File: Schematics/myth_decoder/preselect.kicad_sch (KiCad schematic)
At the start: 8 parts, among them U10 74HC238, U11 74HC238, U12 74LS08, U13 74AHC04, U14 4078, U15 4075, U3 74LS32, U9 74HC238

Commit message: Change d to g
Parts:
- added C1015: C 100nF, Capacitor_THT:C_Disc_D5.0mm_W2.5mm_P2.50mm, symbol Device:C_Small
- added C1016: CP 10μF, Capacitor_THT:CP_Radial_D6.3mm_P2.50mm, symbol Device:C_Polarized_Small
- renumbered U3 to U1003, U9 to U1009, U10 to U1010, U11 to U1011, U12 to U1012, U13 to U1013, U14 to U1014, U15 to U1015
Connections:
- net Vdd: now also C1015.1, C1016.1
- net Vss: now also C1015.2, C1016.2

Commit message: Update pencoder image
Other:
- note added: "NM => END (LOX) NL => NOP (reserved) LM => NOP (reserved) LL => NOP (reserved) MM => NOP (reserved) ML => NOP (reserved) GG => NOP (reserved) RR => NOP (reserved) II => NOP (reserved)"
- note added: "Remap ("scrounge") GG, RR, II etc, and impracticable opcodes such as NM"
- note removed: "NM => END (LOX) NL => NOP (reserved) LM => NOP (reserved) LL => NOP (reserved) MM => NOP (reserved) ML => NOP (reserved) DD => NOP (reserved) RR => NOP (reserved) II => NOP (reserved)"
- note removed: "Remap ("scrounge") DD, RR, II etc, and impracticable opcodes such as NM"
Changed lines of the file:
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@@
 		)
 	)
-	(text "Remap (\"scrounge\") DD, RR, II etc,\nand impracticable opcodes such as NM"
+	(text "Remap (\"scrounge\") GG, RR, II etc,\nand impracticable opcodes such as NM"
 		(exclude_from_sim no)
 		(at 138.43 65.532 0)
@@
 		)
 	)
-	(text "NM => END (LOX)\nNL => NOP (reserved)\nLM => NOP (reserved)\nLL => NOP (reserved)\nMM => NOP (reserved)\nML => NOP (reserved)\nDD => NOP (reserved)\nRR => NOP (reserved)\nII => NOP (reserved)"
+	(text "NM => END (LOX)\nNL => NOP (reserved)\nLM => NOP (reserved)\nLL => NOP (reserved)\nMM => NOP (reserved)\nML => NOP (reserved)\nGG => NOP (reserved)\nRR => NOP (reserved)\nII => NOP (reserved)"
 		(exclude_from_sim no)
 		(at 227.584 64.008 0)

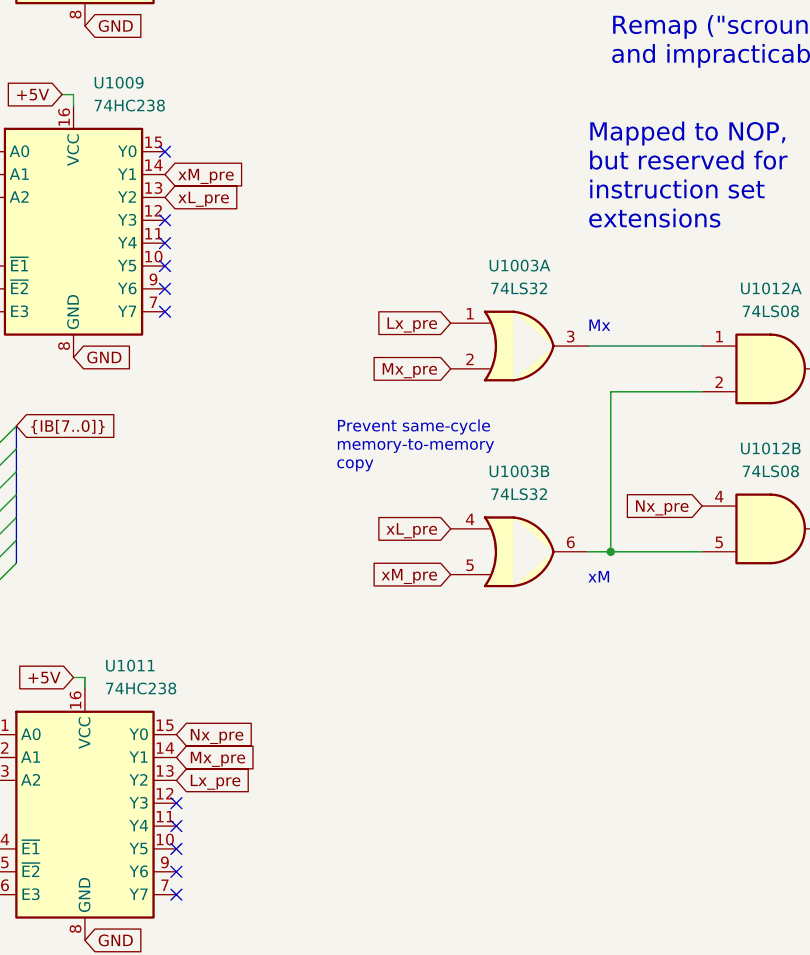
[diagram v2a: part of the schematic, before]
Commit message: Change semantics of xB
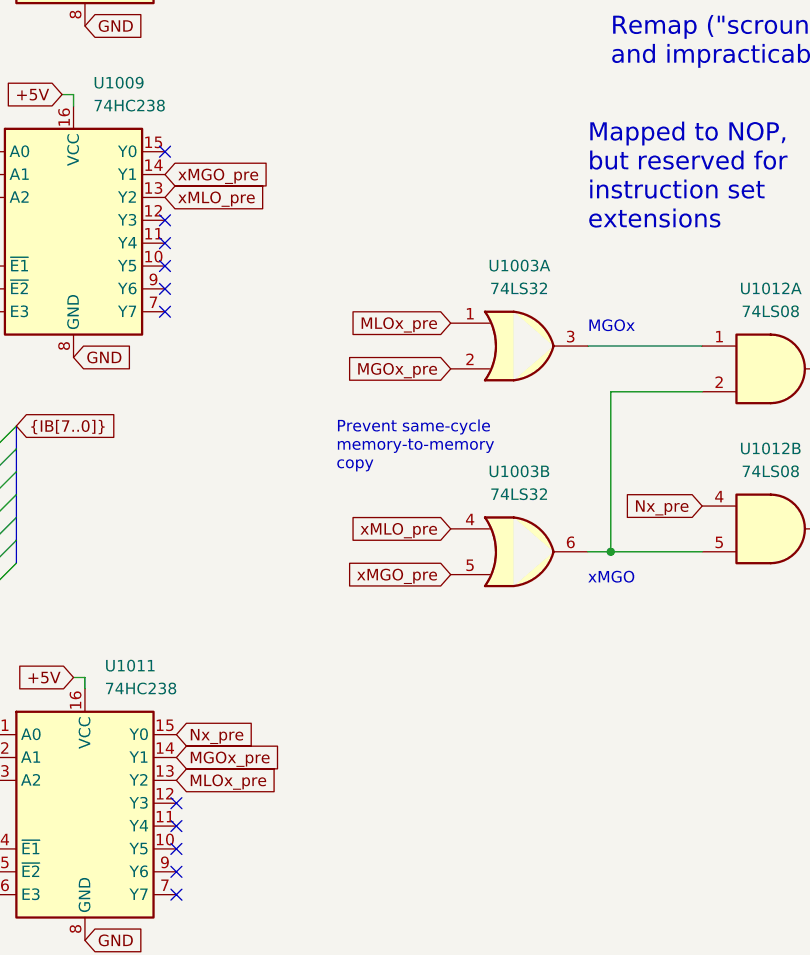
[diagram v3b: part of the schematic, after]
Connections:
- net Lx_pre renamed MLOx_pre
- net Mx_pre renamed MGOx_pre
- net xL_pre renamed xMLO_pre
- net xM_pre renamed xMGO_pre
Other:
- note added: "MGOx"
- note added: "xMGO"
- note removed: "Mx"
- note removed: "xM"
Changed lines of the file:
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@@
 		)
 	)
-	(text "Mx"
+	(text "MGOx"
 		(exclude_from_sim no)
 		(at 135.89 95.25 0)
@@
 		)
 	)
-	(text "xM"
+	(text "xMGO"
 		(exclude_from_sim no)
 		(at 135.89 123.19 0)
@@
 		)
 	)
-	(global_label "Mx_pre"
+	(global_label "MGOx_pre"
 		(shape input)
 		(at 90.17 142.24 0)
@@
 		)
 	)
-	(global_label "Mx_pre"
+	(global_label "MGOx_pre"
 		(shape input)
 		(at 120.65 99.06 180)
@@
 		)
 	)
-	(global_label "Lx_pre"
+	(global_label "MLOx_pre"
 		(shape input)
 		(at 90.17 144.78 0)
@@
 		)
 	)
-	(global_label "xL_pre"
+	(global_label "xMLO_pre"
 		(shape input)
 		(at 88.9 80.01 0)
@@
 		)
 	)
-	(global_label "xM_pre"
+	(global_label "xMGO_pre"
 		(shape input)
 		(at 88.9 77.47 0)
@@
 		)
 	)
-	(global_label "xL_pre"
+	(global_label "xMLO_pre"
 		(shape input)
 		(at 120.65 116.84 180)
@@
 		)
 	)
-	(global_label "xM_pre"
+	(global_label "xMGO_pre"
 		(shape input)
 		(at 120.65 121.92 180)
@@
 		)
 	)
-	(global_label "Lx_pre"
+	(global_label "MLOx_pre"
 		(shape input)
 		(at 120.65 93.98 180)

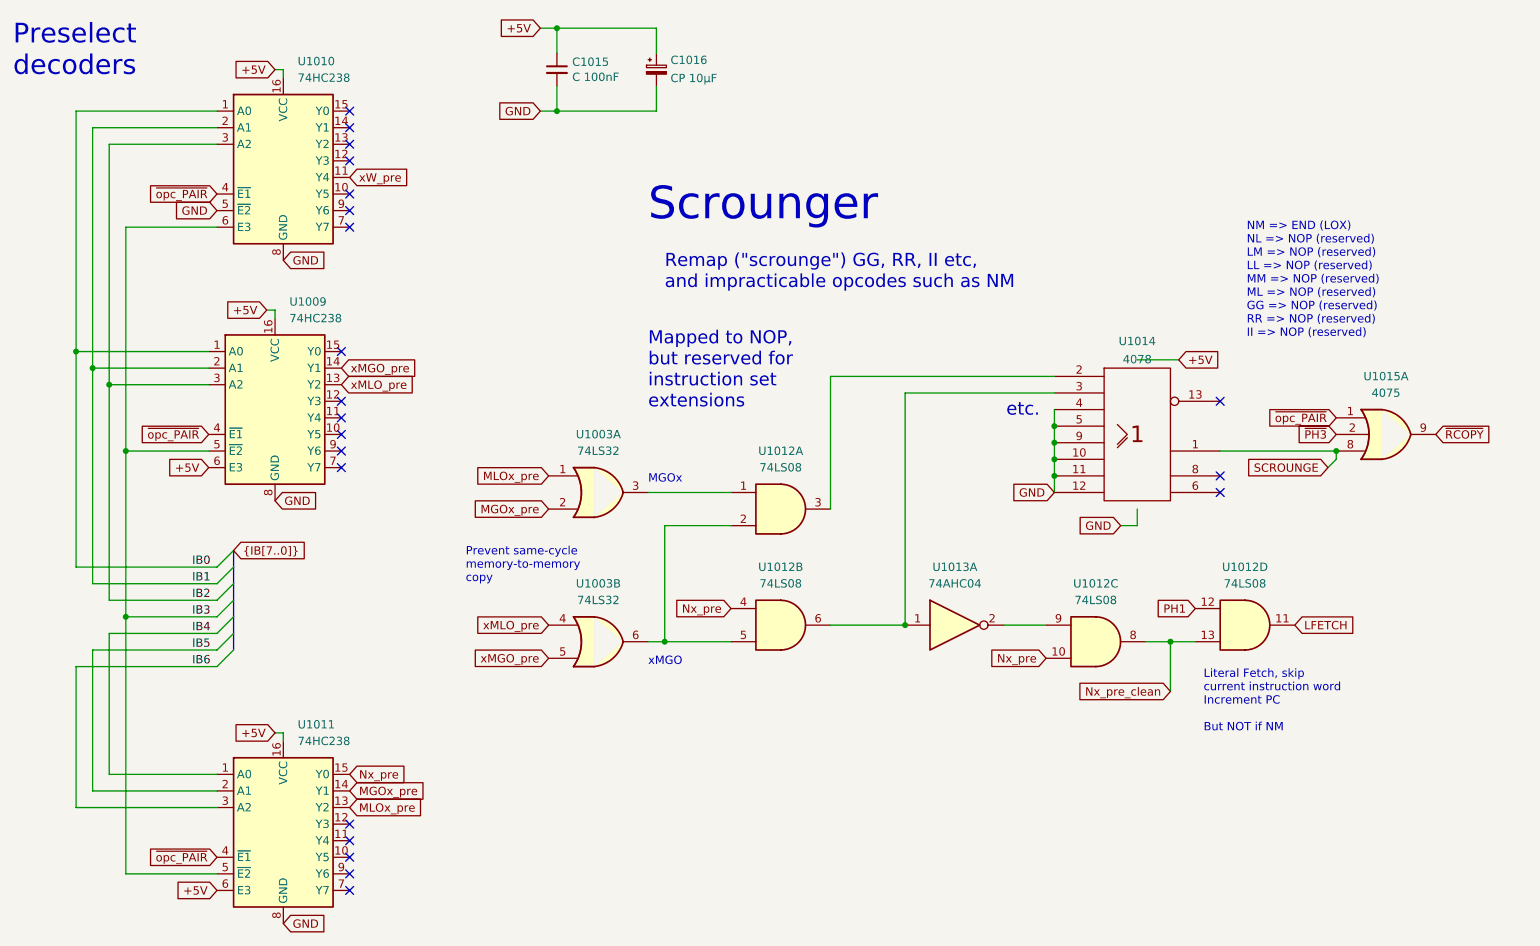
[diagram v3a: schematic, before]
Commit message: Change signal names
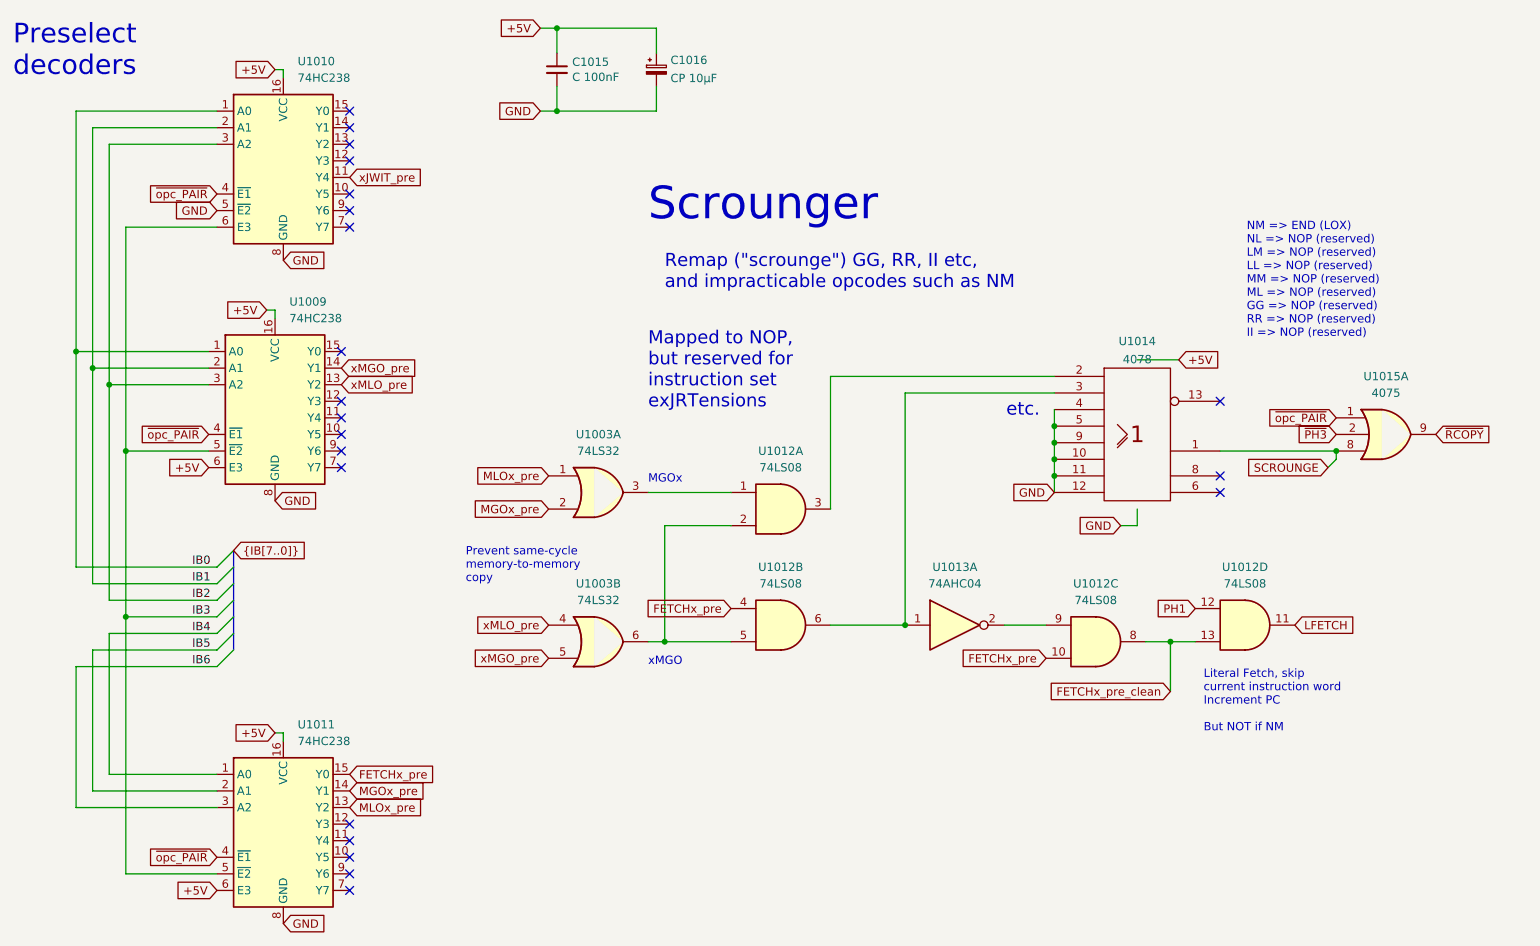
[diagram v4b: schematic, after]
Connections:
- net Nx_pre renamed FETCHx_pre
- net Nx_pre_clean renamed FETCHx_pre_clean
- net xW_pre renamed xJWIT_pre
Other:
- note added: "Mapped to NOP, but reserved for instruction set exJRTensions"
- note removed: "Mapped to NOP, but reserved for instruction set extensions"
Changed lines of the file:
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@@
 		)
 	)
-	(text "Mapped to NOP,\nbut reserved for\ninstruction set\nextensions"
+	(text "Mapped to NOP,\nbut reserved for\ninstruction set\nexJRTensions"
 		(exclude_from_sim no)
 		(at 135.89 83.82 0)
@@
 		)
 	)
-	(global_label "Nx_pre"
+	(global_label "FETCHx_pre"
 		(shape input)
 		(at 196.85 121.92 180)
@@
 		)
 	)
-	(global_label "xW_pre"
+	(global_label "xJWIT_pre"
 		(shape input)
 		(at 90.17 48.26 0)
@@
 		)
 	)
-	(global_label "Nx_pre"
+	(global_label "FETCHx_pre"
 		(shape input)
 		(at 148.59 114.3 180)
@@
 		)
 	)
-	(global_label "Nx_pre"
+	(global_label "FETCHx_pre"
 		(shape input)
 		(at 90.17 139.7 0)
@@
 		)
 	)
-	(global_label "Nx_pre_clean"
+	(global_label "FETCHx_pre_clean"
 		(shape input)
 		(at 215.9 127 180)

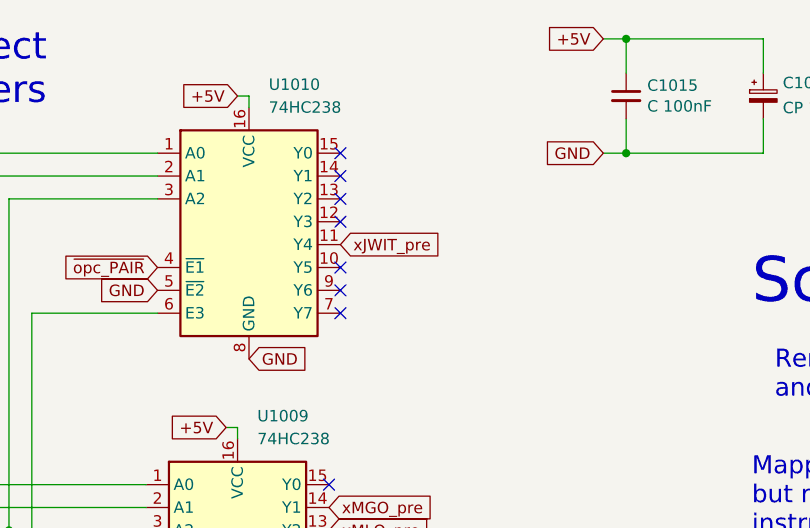
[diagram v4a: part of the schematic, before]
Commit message: Let defines/labels diverge from assembler mnemonics
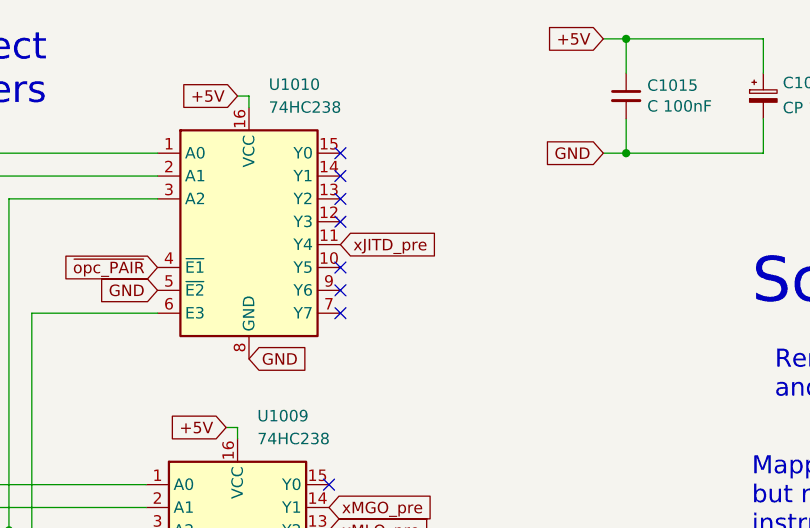
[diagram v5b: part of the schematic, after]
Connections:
- net xJWIT_pre renamed xJITD_pre
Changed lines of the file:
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@@
 		)
 	)
-	(global_label "xJWIT_pre"
+	(global_label "xJITD_pre"
 		(shape input)
 		(at 90.17 48.26 0)
